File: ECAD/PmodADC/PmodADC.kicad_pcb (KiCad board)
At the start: 4 copper layers, 59.1 x 80 mm, 176 parts, among them J1 AudioIn, J2 LeaderTech SMS405, J3 Pmod, J4 AudioOut, SW1 Bypass, SW2 Bypass, U1 74VHCT595BQ-Q100, U10 LM337_SOT223, U11 TLV172IDCK, U12 74VHCT595BQ-Q100, U13 74VHCT595BQ-Q100, U14 74AHCV541ABQ, U15 74AHCV541ABQ, U16 LF398_SOIC8, U17 TLV172IDCK, U18 TLV172IDCK, U19 LMV7235, U2 74VHCT595BQ-Q100, U3 MC34063AD, U4 MC34063AD, U5 74AHCV541ABQ, U6 74AHCV541ABQ, U7 MAX6071BAUT50+T, U8 L7805, U9 LM317_SOT-223

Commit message: Quickfix PCB v0.1
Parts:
- added C45: 1u, Capacitor_SMD:C_0402_1005Metric, F.Cu at (0.00, -127.0)
- added C46: 0u1, Capacitor_SMD:C_0402_1005Metric, F.Cu at (-1.27, -127.0)
- added R79: 100R, Resistor_SMD:R_0402_1005Metric, F.Cu at (-2.54, -127.0)
- added U20: 74AHCT541BQ,115, SOT764-1_DHVQFN20:SOT764-1_DHVQFN20, F.Cu at (-6.35, -125.1)
- C10, C13, C14, C15, C20, C21, C22, C23, C24, C26, C28, C29, C3, C35, C36, C38, C39, C40, C42, C43, C44, C5, C7, C9: value 100n -> 0u1
- C11: value 1000uF -> 1000u
- C12: value 1000uf -> 1000u
- C27, C37: footprint Capacitor_SMD:C_0805_2012Metric -> Capacitor_THT:CP_Radial_D5.0mm_P2.00mm
- C31, C33: value 100nf -> 0u1
- C8: value 470pf -> 470p
- D3: value LED -> Green
- U1, U12, U13, U2: value 74VHCT595BQ-Q100 -> 74VHC595BQ,115
- moved C37 11.7 mm to (-29.2, -54.0), turned to 90 degrees
- moved C27 5.24 mm to (12.1, -52.7), turned to 270 degrees
- moved R39 0.64 mm to (6.99, -52.7)
- moved J4 0.64 mm to (-21.6, -51.4)
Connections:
- net /COMP renamed /COMP_3V
- J3 pad 1: /ADC_L -> /ADC_L_3V
- J3 pad 2: /DAC_L -> /DAC_L_3V
- J3 pad 3: /ADC_C -> /ADC_C_3V
- J3 pad 4: /DAC_C -> /DAC_C_3V
- J3 pad 5: /ADC_S -> /ADC_S_3V
- J3 pad 6: /DAC_S -> /DAC_S_3V
- J3 pad 7: /S&H -> /S&H_3V
- R37 pad 1: Net-(C27-Pad2) -> Net-(C27-Pad1)
- R39 pad 2: Net-(C27-Pad1) -> Net-(C27-Pad2)
- R40 pad 1: Net-(C27-Pad1) -> Net-(C27-Pad2)
- RV3 pad 1: Net-(C37-Pad1) -> Net-(C37-Pad2)
- SW1 pad 1: Net-(C27-Pad1) -> Net-(C27-Pad2)
- SW2 pad 3: Net-(C37-Pad2) -> Net-(C37-Pad1)
- TP14 pad 1: Net-(C37-Pad2) -> Net-(C37-Pad1)
- TP6 pad 1: Net-(C27-Pad1) -> Net-(C27-Pad2)
- U11 pad 4: Net-(C27-Pad2) -> Net-(C27-Pad1)
- U17 pad 3: Net-(C37-Pad2) -> Net-(C37-Pad1)
- U17 pad 4: Net-(C37-Pad2) -> Net-(C37-Pad1)
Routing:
- net Net-(C37-Pad1): track 5.73 -> 38.3 mm
- net /DAC_C: track 66.7 -> 97.2 mm, vias 2 -> 3
- net /DAC_L: track 71.0 -> 98.5 mm, vias 2 -> 3
- net +5V: track 210.8 -> 237.8 mm, vias 13 -> 14
- net /DAC_S: track 61.6 -> 84.1 mm
- net Net-(C37-Pad2): track 38.3 -> 16.7 mm
- net /S&H_3V: track 0.00 -> 21.2 mm
- net /ADC_L: track 59.5 -> 79.0 mm, vias 2 -> 3
- net /DAC_S_3V: track 0.00 -> 16.4 mm
- net /ADC_C_3V: track 0.00 -> 15.8 mm, vias 0 -> 1
- net /ADC_S_3V: track 0.00 -> 15.6 mm
- net Net-(C27-Pad2): track 13.7 -> 29.2 mm
- net /ADC_S: track 65.6 -> 80.5 mm, vias 1 -> 2
- net /DAC_C_3V: track 0.00 -> 13.7 mm
- net /ADC_L_3V: track 0.00 -> 12.5 mm, vias 0 -> 1
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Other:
- board text added: "PmodADC SCHILK v0.1"
- board text removed: "14bit DAC:"
- board text removed: "14bit SAR ADC:"
- board text removed: "PmodADC SCHILK v0.0"

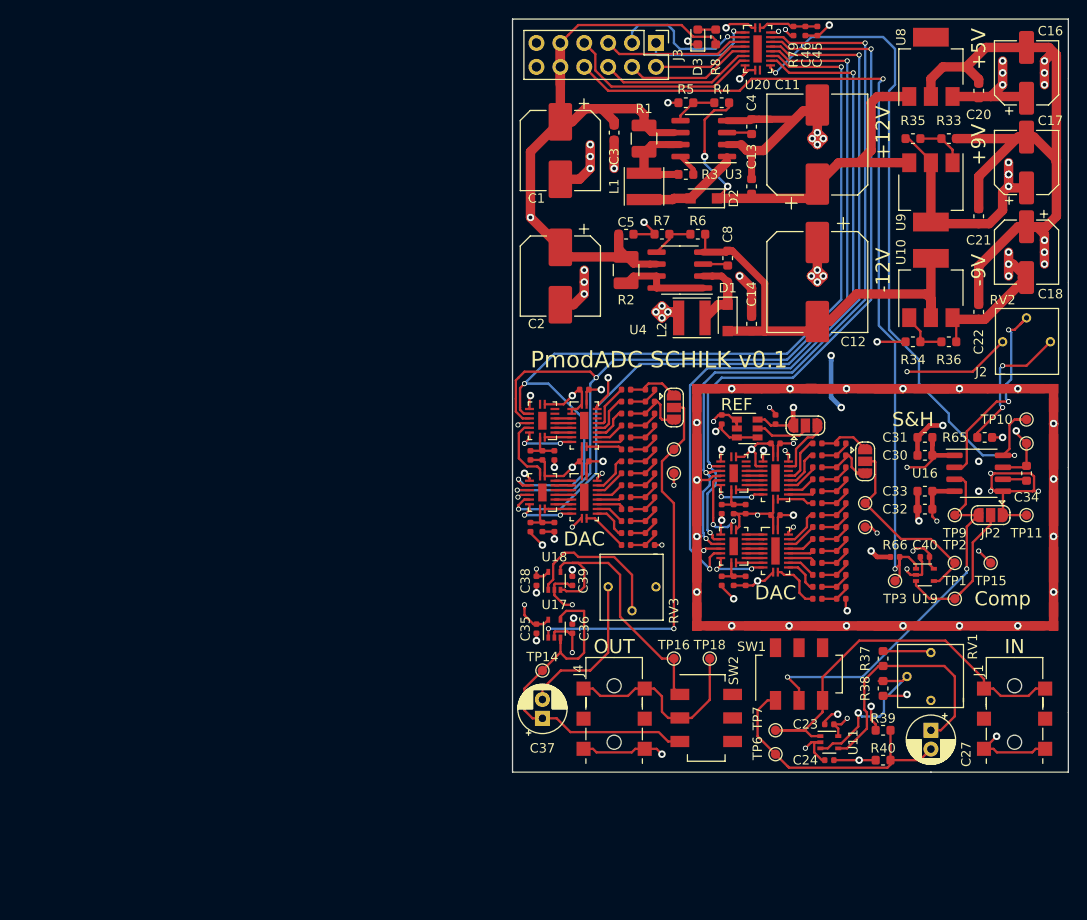
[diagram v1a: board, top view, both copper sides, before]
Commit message: Added Footprints, fixedup Schematic, Cleanup
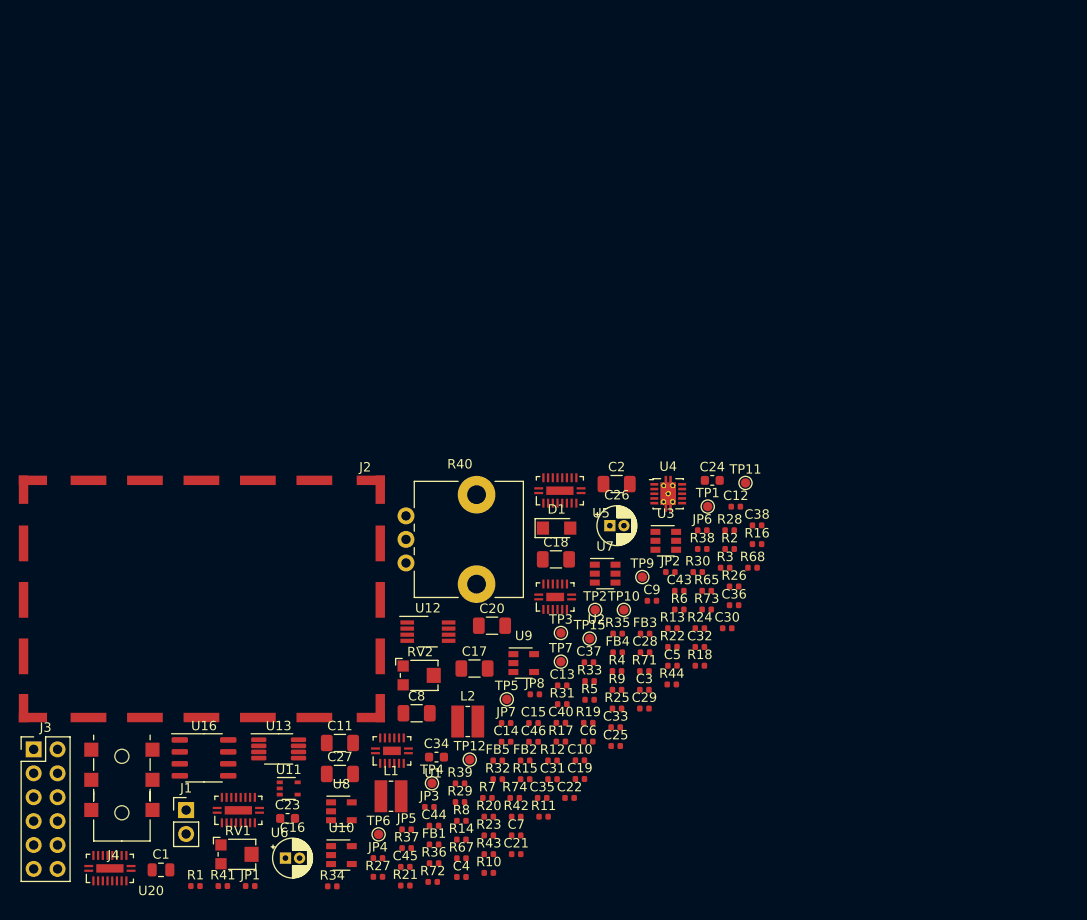
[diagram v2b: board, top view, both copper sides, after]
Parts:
- removed C39, C42: 0u1, Capacitor_SMD:C_0402_1005Metric
- removed C41: 1u, Capacitor_SMD:C_0402_1005Metric
- removed D2: 1N5819, Diode_SMD:D_SOD-123F
- removed D3: Green, Diode_SMD:D_0603_1608Metric
- removed R45, R46, R47, R48, R49, R50, R51, R52, R53, R75, R76: 20K 0.1%, Resistor_SMD:R_0402_1005Metric
- removed R54, R55, R56, R57, R58, R59, R60, R61, R62, R63, R64, R77, R78: 10K 0.1%, Resistor_SMD:R_0402_1005Metric
- removed R66: 10K, Resistor_SMD:R_0402_1005Metric
- removed R69, R70, R79: 100R, Resistor_SMD:R_0402_1005Metric
- removed RV3: 20K, Bourns_3362P:Bourns_3362P
- removed SW1, SW2: Bypass, DPDT_5.6mm_2.5mm_SMD:DPDT_5.6mm_2.5mm_SMD
- removed TP13: DAC, TestPoint:TestPoint_Pad_D1.0mm
- removed TP14: OUT1, TestPoint:TestPoint_Pad_D1.0mm
- removed TP16: OUT2, TestPoint:TestPoint_Pad_D1.0mm
- removed TP18: OUT, TestPoint:TestPoint_Pad_D1.0mm
- removed TP19: GND, TestPoint:TestPoint_Pad_D1.0mm
- removed U14, U15: 74AHCV541ABQ, SOT764-1_DHVQFN20:SOT764-1_DHVQFN20
- removed U17, U18: TLV172IDCK, Package_TO_SOT_SMD:SOT-353_SC-70-5
- removed U19: LMV7235, Package_TO_SOT_SMD:SOT-353_SC-70-5
- added FB1: 1K/100MHz, Inductor_SMD:L_0402_1005Metric, F.Cu at (-40.7, -40.6)
- added FB2: 1K/100MHz, Inductor_SMD:L_0402_1005Metric, F.Cu at (-31.0, -49.5)
- added FB3: 1K/100MHz, Inductor_SMD:L_0402_1005Metric, F.Cu at (-18.3, -63.0)
- added FB4: 1K/100MHz, Inductor_SMD:L_0402_1005Metric, F.Cu at (-21.2, -61.0)
- added FB5: 1K/100MHz, Inductor_SMD:L_0402_1005Metric, F.Cu at (-34.0, -49.5)
- added JP5: DI, Resistor_SMD:R_0402_1005Metric, F.Cu at (-43.6, -42.2)
- added JP6: Normal, Resistor_SMD:R_0402_1005Metric, F.Cu at (-12.2, -74.0)
- added JP7: Jumper, Resistor_SMD:R_0402_1005Metric, F.Cu at (-33.1, -53.5)
- added JP8: DNS, Resistor_SMD:R_0402_1005Metric, F.Cu at (-30.0, -56.5)
- C1: value 100u -> 4u7; footprint Capacitor_SMD:CP_Elec_8x6.5 -> Capacitor_SMD:C_0805_2012Metric
- C11: value 1000u -> 10u; footprint Capacitor_SMD:CP_Elec_10x10.5 -> Capacitor_SMD:C_1206_3216Metric
- C12: value 1000u -> 1u; footprint Capacitor_SMD:CP_Elec_10x10.5 -> Capacitor_SMD:C_0402_1005Metric
- C13, C14: value 0u1 -> 1u; footprint Capacitor_SMD:C_0603_1608Metric -> Capacitor_SMD:C_0402_1005Metric
- C16: footprint Capacitor_SMD:CP_Elec_6.3x7.7 -> Capacitor_THT:CP_Radial_D4.0mm_P1.50mm
- C17, C18: footprint Capacitor_SMD:CP_Elec_6.3x7.7 -> Capacitor_SMD:C_1206_3216Metric
- C2: value 100u -> 10u; footprint Capacitor_SMD:CP_Elec_8x6.5 -> Capacitor_SMD:C_1206_3216Metric
- C20: value 0u1 -> 10u; footprint Capacitor_SMD:C_0603_1608Metric -> Capacitor_SMD:C_1206_3216Metric
- C21, C22, C3, C30, C31, C32, C33: footprint Capacitor_SMD:C_0603_1608Metric -> Capacitor_SMD:C_0402_1005Metric
- C23: value 0u1 -> 10n C0G; footprint Capacitor_SMD:C_0402_1005Metric -> Capacitor_SMD:C_0603_1608Metric
- C24: value 0u1 -> 4n7 C0G; footprint Capacitor_SMD:C_0402_1005Metric -> Capacitor_SMD:C_0603_1608Metric
- C26: value 0u1 -> 10u; footprint Capacitor_SMD:C_0402_1005Metric -> Capacitor_THT:CP_Radial_D4.0mm_P1.50mm
- C27: footprint Capacitor_THT:CP_Radial_D5.0mm_P2.00mm -> Capacitor_SMD:C_1206_3216Metric
- C28, C29, C38: value 0u1 -> 1u
- C34: value 10nF -> 10nF C0G
- C37: value 10u -> DNS; footprint Capacitor_THT:CP_Radial_D5.0mm_P2.00mm -> Capacitor_SMD:C_0402_1005Metric
- C4: value 470p -> 4n7; footprint Capacitor_SMD:C_0603_1608Metric -> Capacitor_SMD:C_0402_1005Metric
- C5: value 0u1 -> 0u22; footprint Capacitor_SMD:C_0603_1608Metric -> Capacitor_SMD:C_0402_1005Metric
- C8: value 470p -> 10u; footprint Capacitor_SMD:C_0603_1608Metric -> Capacitor_SMD:C_1206_3216Metric
- D1: value 1N5819 -> SL03; footprint Diode_SMD:D_SOD-123F -> Diode_SMD:D_SMF
- J1: footprint Jack_3.5mm_PJ-313D-6A:PJ-313D-6A -> Connector_PinHeader_2.54mm:PinHeader_1x02_P2.54mm_Vertical
- J4: value AudioOut -> AudioIn
- JP1: value BitSelect -> byp; footprint Jumper:SolderJumper-3_P1.3mm_Open_RoundedPad1.0x1.5mm -> Resistor_SMD:R_0402_1005Metric
- JP2: value Bypass -> disc; footprint Jumper:SolderJumper-3_P1.3mm_Open_RoundedPad1.0x1.5mm -> Resistor_SMD:R_0402_1005Metric
- JP3: value BitSelect -> disc; footprint Jumper:SolderJumper-3_P1.3mm_Open_RoundedPad1.0x1.5mm -> Resistor_SMD:R_0402_1005Metric
- JP4: value Vref_Feedback -> disc; footprint Jumper:SolderJumper-3_P1.3mm_Open_RoundedPad1.0x1.5mm -> Resistor_SMD:R_0402_1005Metric
- L1, L2: value 22uH 800mA -> 22uH, 300mA; footprint Inductor_SMD:L_Taiyo-Yuden_MD-4040 -> Inductor_SMD:L_Wuerth_MAPI-3020
- R1: value 0R33 / 0.5W -> 10R; footprint Resistor_SMD:R_1210_3225Metric -> Resistor_SMD:R_0402_1005Metric
- R2: value 0R33 / 0.5W -> 120k; footprint Resistor_SMD:R_1210_3225Metric -> Resistor_SMD:R_0402_1005Metric
- R3: value 180R -> 68k; footprint Resistor_SMD:R_0603_1608Metric -> Resistor_SMD:R_0402_1005Metric
- R33: value 1K5 -> 15k; footprint Resistor_SMD:R_0603_1608Metric -> Resistor_SMD:R_0402_1005Metric
- R34: value 1K5 -> 47k; footprint Resistor_SMD:R_0603_1608Metric -> Resistor_SMD:R_0402_1005Metric
- R35, R36: value 240R -> 15k; footprint Resistor_SMD:R_0603_1608Metric -> Resistor_SMD:R_0402_1005Metric
- R37: value 100R -> 47k; footprint Resistor_SMD:R_0603_1608Metric -> Resistor_SMD:R_0402_1005Metric
- R38: value 10K -> 10k; footprint Resistor_SMD:R_0603_1608Metric -> Resistor_SMD:R_0402_1005Metric
- R39: value 10K -> 5k; footprint Resistor_SMD:R_0603_1608Metric -> Resistor_SMD:R_0402_1005Metric
- R4: value 12K -> 5k6; footprint Resistor_SMD:R_0603_1608Metric -> Resistor_SMD:R_0402_1005Metric
- R40: value 10K -> 50k Log; footprint Resistor_SMD:R_0603_1608Metric -> Potentiometer_THT:Potentiometer_Alps_RK09L_Single_Vertical
- R41, R42: value 20K 0.1% -> 1k2
- R43, R44: value 20K 0.1% -> 20k
- R5: value 1K5 -> 560k; footprint Resistor_SMD:R_0603_1608Metric -> Resistor_SMD:R_0402_1005Metric
- R6: value 12K -> 33k; footprint Resistor_SMD:R_0603_1608Metric -> Resistor_SMD:R_0402_1005Metric
- R65: footprint Resistor_SMD:R_0603_1608Metric -> Resistor_SMD:R_0402_1005Metric
- R7: value 1K5 -> 100R; footprint Resistor_SMD:R_0603_1608Metric -> Resistor_SMD:R_0402_1005Metric
- R8: value 22K -> 100k; footprint Resistor_SMD:R_0603_1608Metric -> Resistor_SMD:R_0402_1005Metric
- RV1: value 47K -> 1K; footprint Bourns_3362P:Bourns_3362P -> Potentiometer_SMD:Potentiometer_Bourns_TC33X_Vertical
- RV2: footprint Bourns_3362P:Bourns_3362P -> Potentiometer_SMD:Potentiometer_Bourns_TC33X_Vertical
- TP3: value Comp -> IN
- TP6: value PREA -> IN
- TP7: value IN -> GND
- U10: value LM337_SOT223 -> MIC5270BM5; footprint Package_TO_SOT_SMD:SOT-223-3_TabPin2 -> Package_TO_SOT_SMD:SOT-23-5
- U11: value TLV172IDCK -> SN74LVC1G17DCK
- U12: value 74VHC595BQ,115 -> OPA1602; footprint SOT763-1_DHVQFN16:SOT763-1_DHVQFN16 -> Package_SO:VSSOP-8_3.0x3.0mm_P0.65mm
- U13: value 74VHC595BQ,115 -> LT1711xMS8; footprint SOT763-1_DHVQFN16:SOT763-1_DHVQFN16 -> Package_SO:MSOP-8_3x3mm_P0.65mm
- U3: value MC34063AD -> TLV61046ADB; footprint Package_SO:SOIC-8_3.9x4.9mm_P1.27mm -> Package_TO_SOT_SMD:SOT-23-6
- U4: value MC34063AD -> TPS63700; footprint Package_SO:SOIC-8_3.9x4.9mm_P1.27mm -> Package_SON:VSON-10-1EP_3x3mm_P0.5mm_EP1.65x2.4mm_ThermalVias
- U7: value MAX6071BAUT50+T -> REF3450
- U8: value L7805 -> LDK320AM-R; footprint Package_TO_SOT_SMD:SOT-223 -> Package_TO_SOT_SMD:SOT-23-5
- U9: value LM317_SOT-223 -> LDK320AM-R; footprint Package_TO_SOT_SMD:SOT-223-3_TabPin2 -> Package_TO_SOT_SMD:SOT-23-5
- moved C16 114.7 mm to (-56.5, -39.1), turned to 0 degrees
- moved U20 111.0 mm to (-75.2, -38.0), turned to 0 degrees
- moved U8 100.9 mm to (-50.6, -44.1), turned to 0 degrees
- moved J3 100.0 mm to (-83.3, -50.7), turned to 0 degrees
- moved C45 99.0 mm to (-43.8, -38.2), turned to 0 degrees
- moved R1 92.6 mm to (-66.1, -36.2), turned to 0 degrees
- moved J1 88.3 mm to (-67.1, -44.2), turned to 0 degrees
- moved U16 87.7 mm to (-65.2, -49.8)
- moved R8 87.6 mm to (-37.8, -43.1), turned to 0 degrees
- moved C1 87.4 mm to (-69.7, -37.9), turned to 0 degrees
- moved U10 86.9 mm to (-50.6, -39.4), turned to 0 degrees
- moved C4 85.5 mm to (-37.8, -37.1), turned to 0 degrees
- moved R34 84.6 mm to (-51.5, -36.1), turned to 0 degrees
- moved C21 83.7 mm to (-32.0, -39.5), turned to 0 degrees
- moved C11 81.3 mm to (-50.7, -51.4), turned to 0 degrees
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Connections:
- C13 pad 1: Net-(C11-Pad1) -> GND
- C13 pad 2: GND -> Net-(C12-Pad2)
- C14 pad 1: Net-(C12-Pad2) -> Net-(C11-Pad1)
- C16 pad 1: +5V -> Net-(C16-Pad1)
- C16 pad 2: GND -> /DI
- C17 pad 1: +9V -> Net-(C17-Pad1)
- C18 pad 1: GND -> Net-(C18-Pad1)
- C18 pad 2: -9V -> GND
- C20 pad 1: +5V -> GND
- C20 pad 2: GND -> Net-(C20-Pad2)
- C21 pad 1: +9V -> +3V3
- C22 pad 2: -9V -> +5VA
- C23 pad 1: GND -> Net-(C23-Pad1)
- C23 pad 2: +9V -> Net-(C23-Pad2)
- C24 pad 2: -9V -> Net-(C24-Pad2)
- C25 pad 1: Net-(C25-Pad1) -> /Vref_5V
- C26 pad 1: Net-(C25-Pad1) -> Net-(C26-Pad1)
- C26 pad 2: GND -> Net-(C23-Pad1)
- C27 pad 1: Net-(C27-Pad1) -> /Vref_5V
- C27 pad 2: Net-(C27-Pad2) -> GND
- C28 pad 1: /Vref_5V -> +9V
- C29 pad 1: /Vref_5V -> GND
- C29 pad 2: GND -> -5V
- C3 pad 1: +3V3 -> GND
- C3 pad 2: GND -> Net-(C3-Pad2)
- C32 pad 1: -9V -> -5V
- C33 pad 1: -9V -> -5V
- C35 pad 1: GND -> +9V
- C35 pad 2: +9V -> GND
- C36 pad 2: -9V -> -5V
- C37 pad 2: Net-(C37-Pad2) -> GND
- C38 pad 1: GND -> +5V
- C38 pad 2: +9V -> GND
- C4 pad 1: Net-(C4-Pad1) -> GND
- C4 pad 2: GND -> Net-(C4-Pad2)
- C44 pad 1: /Vref_5V -> Net-(C44-Pad1)
- C5 pad 1: +3V3 -> GND
- C5 pad 2: GND -> Net-(C5-Pad2)
- C8 pad 1: Net-(C8-Pad1) -> Net-(C12-Pad2)
- C8 pad 2: Net-(C12-Pad2) -> GND
- D1 pad 2: Net-(C12-Pad2) -> Net-(C11-Pad1)
- J3 pad 10: +3V3 -> GND
- J3 pad 11: GND -> +3V3
- J3 pad 12: GND -> +3V3
- J3 pad 2: /DAC_L_3V -> Net-(J3-Pad2)
- J3 pad 4: /DAC_C_3V -> Net-(J3-Pad4)
- J3 pad 6: /DAC_S_3V -> /COMP_L_3V
- J3 pad 9: +3V3 -> GND
- J4 pad R: (no net) -> Net-(J4-PadR)
- J4 pad T: Net-(J4-PadT) -> Net-(C16-Pad1)
- JP1 pad 1: Net-(JP1-Pad1) -> Net-(C16-Pad1)
- JP1 pad 2: Net-(JP1-Pad2) -> /DI
- JP2 pad 1: Net-(JP2-Pad1) -> Net-(C17-Pad1)
- JP2 pad 2: Net-(JP2-Pad2) -> +9V
- JP3 pad 1: Net-(JP3-Pad1) -> Net-(C18-Pad1)
- JP3 pad 2: Net-(JP3-Pad2) -> +5V
- JP4 pad 1: /Vref_5V -> Net-(C20-Pad2)
- JP4 pad 2: Net-(JP4-Pad2) -> -5V
- L1 pad 1: Net-(L1-Pad1) -> +3V3
- R1 pad 1: Net-(L1-Pad1) -> +3V3
- R1 pad 2: +3V3 -> Net-(C3-Pad2)
- R2 pad 2: +3V3 -> Net-(C5-Pad2)
- R21 pad 1: Net-(JP1-Pad3) -> Net-(R21-Pad1)
- R3 pad 1: Net-(L1-Pad1) -> Net-(C12-Pad2)
- R32 pad 2: Net-(JP1-Pad3) -> Net-(R21-Pad1)
- R33 pad 1: GND -> Net-(R33-Pad1)
- R33 pad 2: Net-(R33-Pad2) -> GND
- R34 pad 1: Net-(R34-Pad1) -> Net-(C18-Pad1)
- R34 pad 2: GND -> Net-(R34-Pad2)
- R35 pad 1: Net-(R33-Pad2) -> Net-(R34-Pad2)
- R35 pad 2: +9V -> GND
- R36 pad 1: -9V -> Net-(R36-Pad1)
- R36 pad 2: Net-(R34-Pad1) -> GND
- R37 pad 1: Net-(C27-Pad1) -> Net-(C20-Pad2)
- R37 pad 2: Net-(R37-Pad2) -> Net-(R36-Pad1)
- R38 pad 1: Net-(R38-Pad1) -> /DI
- R39 pad 1: +5V -> GND
- R39 pad 2: Net-(C27-Pad2) -> Net-(R39-Pad2)
- R4 pad 1: Net-(R4-Pad1) -> Net-(R3-Pad2)
- R4 pad 2: Net-(C11-Pad1) -> GND
- R40 pad 1: Net-(C27-Pad2) -> Net-(R40-Pad1)
- R40 pad 2: GND -> Net-(R39-Pad2)
- R41 pad 1: Net-(R41-Pad1) -> Net-(C23-Pad2)
- R41 pad 2: GND -> Net-(R40-Pad1)
- R42 pad 1: Net-(R41-Pad1) -> Net-(C24-Pad2)
- R42 pad 2: Net-(R42-Pad2) -> Net-(C23-Pad2)
- R43 pad 2: Net-(R43-Pad2) -> /Vref_5V
- R44 pad 1: Net-(R44-Pad1) -> GND
- R5 pad 1: GND -> Net-(R5-Pad1)
- R5 pad 2: Net-(R4-Pad1) -> Net-(R2-Pad1)
- R6 pad 1: Net-(R6-Pad1) -> Net-(C11-Pad1)
- R6 pad 2: Net-(C12-Pad2) -> Net-(R5-Pad1)
- R67 pad 1: +5V -> Net-(FB3-Pad2)
- R68 pad 1: +5V -> Net-(FB4-Pad2)
- R7 pad 1: GND -> Net-(FB1-Pad2)
- R7 pad 2: Net-(R6-Pad1) -> Net-(C45-Pad1)
- R72 pad 1: Net-(JP1-Pad1) -> Net-(C37-Pad1)
- R73 pad 1: Net-(JP1-Pad3) -> Net-(R21-Pad1)
- R74 pad 2: Net-(JP1-Pad1) -> Net-(C37-Pad1)
- R8 pad 1: +3V3 -> Net-(C17-Pad1)
- R8 pad 2: Net-(D3-Pad2) -> Net-(R33-Pad1)
- RV1 pad 1: Net-(R37-Pad2) -> Net-(R43-Pad1)
- RV1 pad 2: Net-(R38-Pad1) -> Net-(C26-Pad1)
- RV1 pad 3: (no net) -> Net-(R44-Pad2)
- TP1 pad 1: Net-(JP2-Pad2) -> Net-(JP7-Pad2)
- TP11 pad 1: Net-(JP2-Pad1) -> Net-(JP7-Pad1)
- TP2 pad 1: Net-(JP1-Pad2) -> Net-(C37-Pad1)
- TP3 pad 1: /COMP_3V -> Net-(C16-Pad1)
- TP5 pad 1: Net-(JP1-Pad2) -> Net-(C37-Pad1)
- TP6 pad 1: Net-(C27-Pad2) -> Net-(C26-Pad1)
- TP7 pad 1: Net-(J1-PadT) -> GND
- TP9 pad 1: Net-(JP2-Pad3) -> Net-(JP5-Pad2)
- U10 pad 1: Net-(R34-Pad1) -> (no net)
- U10 pad 2: Net-(C12-Pad2) -> GND
- U10 pad 3: -9V -> Net-(U10-Pad3)
- U11 pad 1: Net-(J1-PadT) -> (no net)
- U11 pad 2: -9V -> /COMP
- U11 pad 3: Net-(R38-Pad1) -> GND
- U11 pad 4: Net-(C27-Pad1) -> /COMP_3V
- U11 pad 5: +9V -> +3V3
- U12 pad 1: Net-(U12-Pad1) -> Net-(R40-Pad1)
- U12 pad 2: Net-(U12-Pad2) -> Net-(R39-Pad2)
- U12 pad 3: Net-(U12-Pad3) -> /DI
- U12 pad 4: Net-(U12-Pad4) -> -5V
- U12 pad 5: Net-(U12-Pad5) -> Net-(C24-Pad2)
- U12 pad 6: Net-(U12-Pad6) -> Net-(C23-Pad1)
- U12 pad 7: Net-(U12-Pad7) -> Net-(C23-Pad1)
- U12 pad 8: GND -> +9V
- U13 pad 1: Net-(U13-Pad1) -> +5V
- U13 pad 2: Net-(U13-Pad2) -> Net-(JP7-Pad2)
- U13 pad 3: Net-(U13-Pad3) -> Net-(C37-Pad1)
- U13 pad 4: Net-(U13-Pad4) -> GND
- U13 pad 5: Net-(U13-Pad5) -> /COMP_L_5v
- U13 pad 6: Net-(U13-Pad6) -> GND
- U13 pad 7: Net-(U13-Pad7) -> /COMP
- U13 pad 8: GND -> Net-(U13-Pad8)
- U16 pad 3: Net-(JP2-Pad3) -> Net-(JP5-Pad2)
- U16 pad 4: -9V -> -5V
- U16 pad 5: Net-(JP2-Pad1) -> Net-(JP7-Pad1)
- U20 pad 10: GND -> Net-(U20-Pad10)
- U20 pad 12: /S&H -> Net-(U20-Pad12)
- U20 pad 13: /DAC_S -> Net-(U20-Pad13)
- U20 pad 14: /DAC_C -> /COMP_L
- U20 pad 15: /DAC_L -> /S&H
- U20 pad 5: /DAC_L_3V -> /S&H_3V
- U20 pad 6: /DAC_C_3V -> /COMP_L_3V
- U20 pad 7: /DAC_S_3V -> GND
- U20 pad 8: /S&H_3V -> GND
- U3 pad 3: Net-(C4-Pad1) -> Net-(R3-Pad2)
- U3 pad 4: GND -> +3V3
- U3 pad 5: Net-(R4-Pad1) -> Net-(C12-Pad2)
- U4 pad 1: Net-(R2-Pad1) -> Net-(C4-Pad2)
- U4 pad 2: Net-(D1-Pad1) -> GND
- U4 pad 3: Net-(C8-Pad1) -> Net-(C3-Pad2)
- U4 pad 4: Net-(C12-Pad2) -> Net-(C3-Pad2)
- U4 pad 5: Net-(R6-Pad1) -> +3V3
- U4 pad 6: +3V3 -> Net-(D1-Pad1)
- U4 pad 7: Net-(R2-Pad1) -> GND
- U4 pad 8: Net-(R2-Pad1) -> Net-(C11-Pad1)
- U6 pad 18: /Vref_Sense -> Net-(U6-Pad18)
- U6 pad 2: +5V -> GND
- U7 pad 5: Net-(JP4-Pad2) -> Net-(C44-Pad1)
- U7 pad 6: /Vref_5V -> Net-(C44-Pad1)
- U8 pad 1: Net-(C11-Pad1) -> Net-(C12-Pad2)
- U8 pad 3: +5V -> Net-(C12-Pad2)
- U8 pad 4: (no net) -> Net-(R33-Pad1)
- U9 pad 1: Net-(R33-Pad2) -> Net-(C12-Pad2)
- U9 pad 2: +9V -> GND
- U9 pad 3: Net-(C11-Pad1) -> Net-(C12-Pad2)
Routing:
- net GND: track 442.0 -> 0.00 mm, vias 91 -> 0
- net +5V: track 237.8 -> 0.00 mm, vias 14 -> 0
- net +9V: track 231.5 -> 0.00 mm, vias 10 -> 0
- net -9V: track 166.6 -> 0.00 mm, vias 7 -> 0
- net +3V3: track 140.8 -> 0.00 mm, vias 5 -> 0
- net /DAC_L: track 98.5 -> 0.00 mm, vias 3 -> 0
- net /DAC_C: track 97.2 -> 0.00 mm, vias 3 -> 0
- net /COMP_3V: track 93.0 -> 0.00 mm, vias 2 -> 0
- net /DAC_S: track 84.1 -> 0.00 mm, vias 2 -> 0
- net /ADC_S: track 80.5 -> 0.00 mm, vias 2 -> 0
- net /ADC_L: track 79.0 -> 0.00 mm, vias 3 -> 0
- net /ADC_C: track 77.6 -> 0.00 mm, vias 3 -> 0
- net /S&H: track 74.6 -> 0.00 mm, vias 2 -> 0
- net /Vref_5V: track 59.7 -> 0.00 mm, vias 5 -> 0
- net Net-(C12-Pad2): track 46.8 -> 0.00 mm
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- removed copper zone on In1.Cu, net GND
- removed copper zone on In2.Cu, net GND
- removed copper zone on In1.Cu, net Net-(JP2-Pad1)
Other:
- board outline removed
- board text removed: "+12V"
- board text removed: "+5V"
- board text removed: "+9V"
- board text removed: "-12V"
- board text removed: "-9V"
- board text removed: "Comp"
- board text removed: "DAC"
- board text removed: "IN"
- board text removed: "OUT"
- board text removed: "PmodADC SCHILK v0.1"
- board text removed: "REF"
- board text removed: "S&H"
